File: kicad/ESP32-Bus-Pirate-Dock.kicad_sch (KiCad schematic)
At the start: 21 parts, among them J1 Conn_01x10V, J2 Conn_01x22, J3 Conn_01x22, J4 Conn_01x10H, SW1 SW_DP3T, U1 ESP32-S3-DEVKITC-1-N8R2, U2 AMS1117-1.8, U3 FXMA108

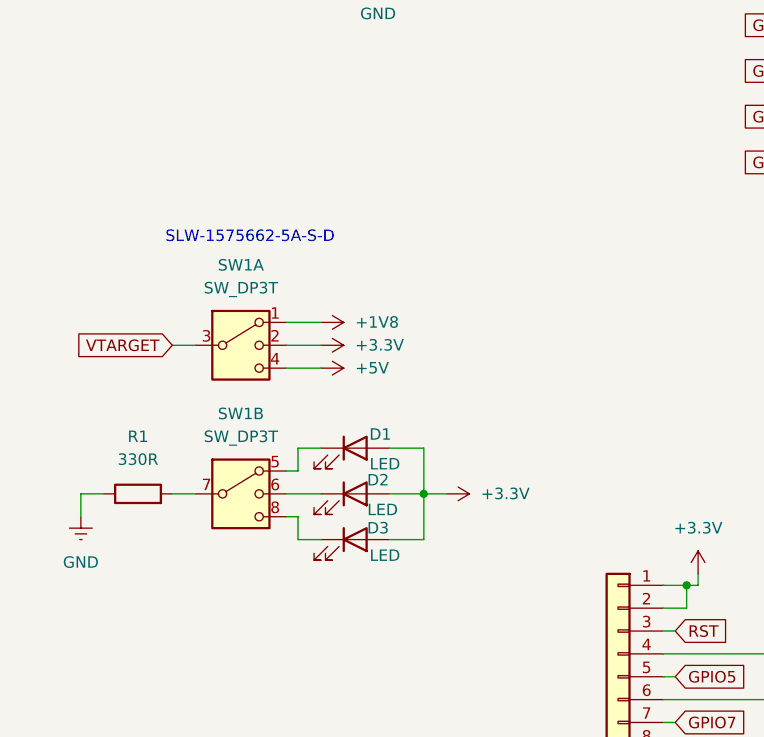
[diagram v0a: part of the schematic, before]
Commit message: Added LEDs for voltage selection and DP3T switch
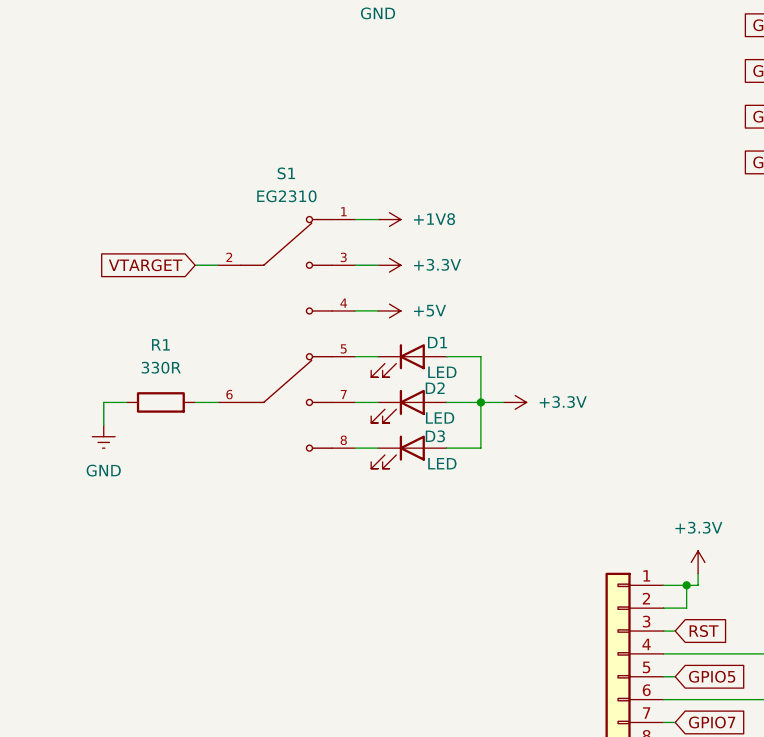
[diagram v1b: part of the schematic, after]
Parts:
- removed SW1: SW_DP3T, symbol Switch:SW_DP3T
- added S1: EG2310, EG2310:SW_EG2310, symbol EG2310:EG2310
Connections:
- net +1V8: now also S1.1
- net +3.3V: now also S1.3
- net +5V: now also S1.4
- net VTARGET: now also S1.2
- net at R1.2: now also S1.6
- net at D3.1 (K): now also S1.8
- net at D1.1 (K): now also S1.5
- net at D2.1 (K): now also S1.7
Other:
- note removed: "SLW-1575662-5A-S-D"
- moved on the sheet: D1, D2, D3, R1

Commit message: Added logo
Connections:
- net GND: now also U3.11 (~{OE})
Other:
- note added: "A. Vladescu"
- note added: "ESP32 Bus Pirate Dock"
- company: (none) -> ESP32 Bus Pirate
- moved on the sheet: H1, H2, H3, H4, J2, J3

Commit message: Excluded vertical header
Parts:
- J1: now not fitted; now left out of the parts list
- J4: footprint Connector_PinSocket_2.54mm:PinSocket_1x10_P2.54mm_Horizontal -> Connector_PinHeader_2.54mm:PinHeader_1x10_P2.54mm_Horizontal
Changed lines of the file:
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@@
 			)
 		)
-		(property "Footprint" "Connector_PinSocket_2.54mm:PinSocket_1x10_P2.54mm_Horizontal"
+		(property "Footprint" "Connector_PinHeader_2.54mm:PinHeader_1x10_P2.54mm_Horizontal"
 			(at 35.56 49.53 0)
 			(effects
@@
 		(unit 1)
 		(exclude_from_sim no)
-		(in_bom yes)
-		(on_board yes)
-		(dnp no)
+		(in_bom no)
+		(on_board yes)
+		(dnp yes)
 		(property "Reference" "J1"
 			(at 48.26 33.274 0)

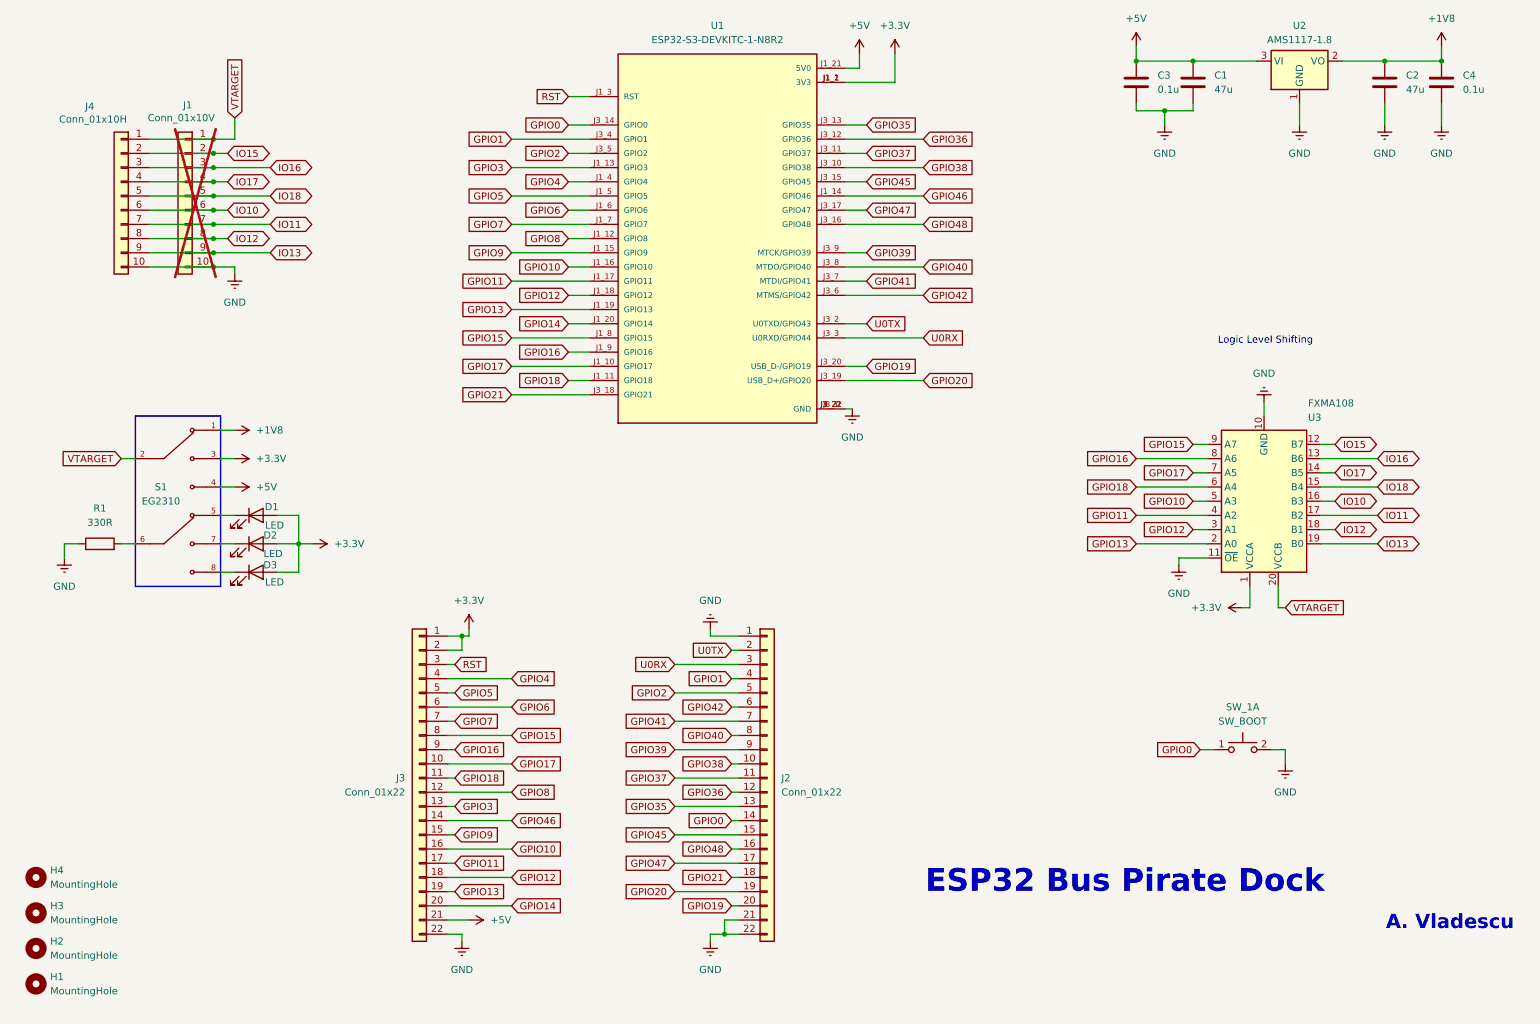
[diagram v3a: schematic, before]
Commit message: Added keyed connector
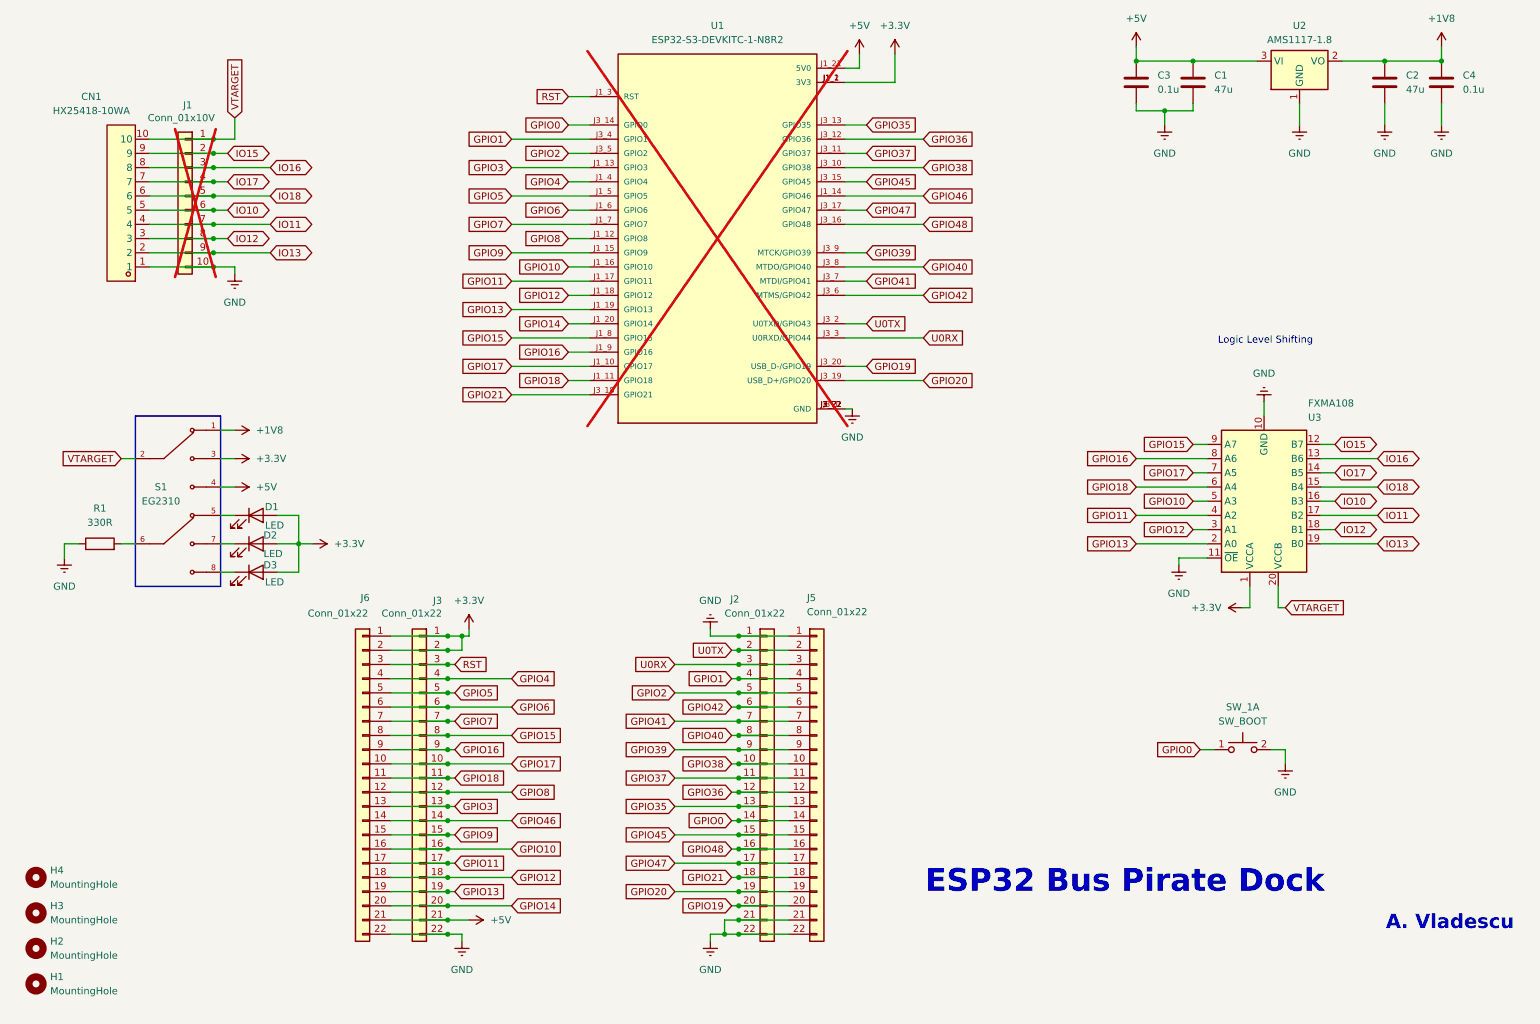
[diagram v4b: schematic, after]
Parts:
- removed J4: Conn_01x10H, Connector_PinHeader_2.54mm:PinHeader_1x10_P2.54mm_Horizontal, symbol Connector_Generic:Conn_01x10
- added CN1: HX25418-10WA, HX25418:CONN-TH_HX25418-10WA, symbol CONN-TH_HX25418-10WA:HX25418-10WA
- added J5, J6: Conn_01x22, Connector_PinSocket_2.54mm:PinSocket_1x22_P2.54mm_Vertical, symbol Connector_Generic:Conn_01x22
- U1: now not fitted; now left out of the parts list
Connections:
- net +3.3V: now also J6.1 (Pin_1), J6.2 (Pin_2)
- net +5V: now also J6.21 (Pin_21)
- net GND: now also CN1.1, J5.1 (Pin_1), J5.21 (Pin_21), J5.22 (Pin_22), J6.22 (Pin_22)
- net GPIO0: now also J5.14 (Pin_14)
- net GPIO1: now also J5.4 (Pin_4)
- net GPIO10: now also J6.16 (Pin_16)
- net GPIO11: now also J6.17 (Pin_17)
- net GPIO12: now also J6.18 (Pin_18)
- net GPIO13: now also J6.19 (Pin_19)
- net GPIO14: now also J6.20 (Pin_20)
- net GPIO15: now also J6.8 (Pin_8)
- net GPIO16: now also J6.9 (Pin_9)
- net GPIO17: now also J6.10 (Pin_10)
- net GPIO18: now also J6.11 (Pin_11)
- net GPIO19: now also J5.20 (Pin_20)
- net GPIO2: now also J5.5 (Pin_5)
- net GPIO20: now also J5.19 (Pin_19)
- net GPIO21: now also J5.18 (Pin_18)
- net GPIO3: now also J6.13 (Pin_13)
- net GPIO35: now also J5.13 (Pin_13)
- net GPIO36: now also J5.12 (Pin_12)
- net GPIO37: now also J5.11 (Pin_11)
- net GPIO38: now also J5.10 (Pin_10)
- net GPIO39: now also J5.9 (Pin_9)
- net GPIO4: now also J6.4 (Pin_4)
- net GPIO40: now also J5.8 (Pin_8)
- net GPIO41: now also J5.7 (Pin_7)
- net GPIO42: now also J5.6 (Pin_6)
- net GPIO45: now also J5.15 (Pin_15)
- net GPIO46: now also J6.14 (Pin_14)
- net GPIO47: now also J5.17 (Pin_17)
- net GPIO48: now also J5.16 (Pin_16)
- net GPIO5: now also J6.5 (Pin_5)
- net GPIO6: now also J6.6 (Pin_6)
- net GPIO7: now also J6.7 (Pin_7)
- net GPIO8: now also J6.12 (Pin_12)
- net GPIO9: now also J6.15 (Pin_15)
- net IO10: now also CN1.5
- net IO11: now also CN1.4
- net IO12: now also CN1.3
- net IO13: now also CN1.2
- net IO15: now also CN1.9
- net IO16: now also CN1.8
- net IO17: now also CN1.7
- net IO18: now also CN1.6
- net RST: now also J6.3 (Pin_3)
- net U0RX: now also J5.3 (Pin_3)
- net U0TX: now also J5.2 (Pin_2)
- net VTARGET: now also CN1.10

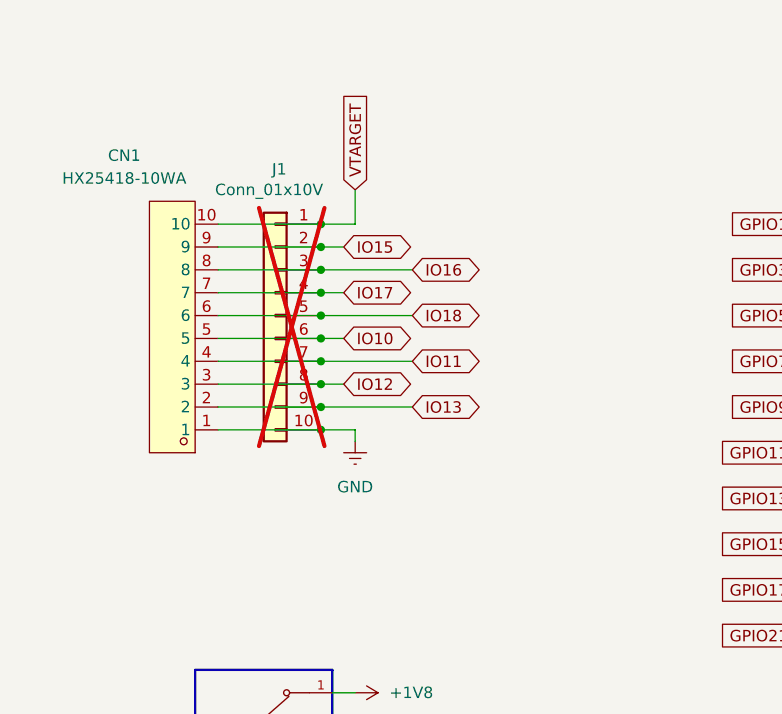
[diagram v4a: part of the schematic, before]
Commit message: Fixed connector polarity
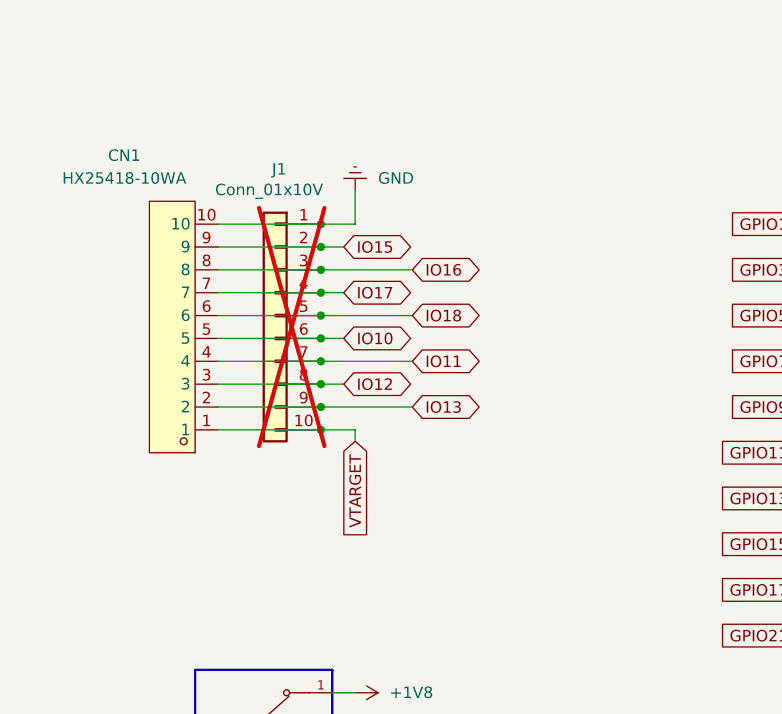
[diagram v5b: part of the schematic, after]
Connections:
- net GND: now also CN1.10, J1.1 (Pin_1); no longer CN1.1, J1.10 (Pin_10)
- net VTARGET: now also CN1.1, J1.10 (Pin_10); no longer CN1.10, J1.1 (Pin_1)
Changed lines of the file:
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@@
 		)
 	)
+	(global_label "VTARGET"
+		(shape input)
+		(at 55.88 63.5 270)
+		(fields_autoplaced yes)
+		(effects
+			(font
+				(size 1.27 1.27)
+			)
+			(justify right)
+		)
+		(property "Intersheetrefs" "${INTERSHEET_REFS}"
+			(at 55.88 74.2866 90)
+			(effects
+				(font
+					(size 1.27 1.27)
+				)
+				(justify right)
+				(hide yes)
+			)
+		)
+	)
 	(global_label "GPIO37"
 		(shape input)
@@
 		)
 	)
-	(global_label "VTARGET"
-		(shape input)
-		(at 55.88 35.56 90)
-		(fields_autoplaced yes)
-		(effects
-			(font
-				(size 1.27 1.27)
-			)
-			(justify left)
-		)
-		(property "Intersheetrefs" "${INTERSHEET_REFS}"
-			(at 55.88 24.7734 90)
-			(effects
-				(font
-					(size 1.27 1.27)
-				)
-				(justify left)
-				(hide yes)
-			)
-		)
-	)
 	(global_label "GPIO10"
 		(shape input)
@@
 	(symbol
 		(lib_id "power:Earth")
-		(at 55.88 63.5 0)
+		(at 55.88 35.56 180)
 		(unit 1)
 		(exclude_from_sim no)
@@
 		(fields_autoplaced yes)
 		(property "Reference" "#PWR02"
-			(at 55.88 69.85 0)
+			(at 55.88 29.21 0)
 			(effects
 				(font
@@
 		)
 		(property "Value" "GND"
-			(at 55.88 68.58 0)
+			(at 58.42 34.2899 0)
 			(effects
 				(font
 					(size 1.27 1.27)
 				)
+				(justify right)
 			)
 		)
 		(property "Footprint" ""
-			(at 55.88 63.5 0)
+			(at 55.88 35.56 0)
 			(effects
 				(font
@@
 		)
 		(property "Datasheet" "~"
-			(at 55.88 63.5 0)
+			(at 55.88 35.56 0)
 			(effects
 				(font
@@
 		)
 		(property "Description" "Power symbol creates a global label with name \"Earth\""
-			(at 55.88 63.5 0)
+			(at 55.88 35.56 0)
 			(effects
 				(font
@@
 		(exclude_from_sim no)
 		(in_bom no)
-		(on_board yes)
+		(on_board no)
 		(dnp yes)
 		(fields_autoplaced yes)
@@
 		(exclude_from_sim no)
 		(in_bom no)
-		(on_board yes)
+		(on_board no)
 		(dnp yes)
 		(property "Reference" "J1"

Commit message: Scheme organization
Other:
- note removed: "A. Vladescu"
- moved on the sheet: C1, C2, C3, C4, SW_1A, U2

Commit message: PCBWay recommendation
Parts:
- C1, C2: value 47u -> 4.7u
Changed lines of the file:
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@@
 			)
 		)
-		(property "Value" "47u"
+		(property "Value" "4.7u"
 			(at 262.89 35.5599 0)
 			(effects
@@
 			)
 		)
-		(property "Value" "47u"
+		(property "Value" "4.7u"
 			(at 228.6 35.5599 0)
 			(effects

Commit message: PCB reassignment
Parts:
- H1, H2, H3, H4: footprint MountingHole:MountingHole_3.2mm_M3 -> MountingHole:MountingHole_3.2mm_M3_DIN965_Pad_TopBottom
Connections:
- net D3: now reaches D3.1 (K), S1.8
- net D1: now reaches D1.1 (K), S1.5
- net D2: now reaches D2.1 (K), S1.7
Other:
- moved on the sheet: C1, C2, C3, C4, D1, D2, D3
